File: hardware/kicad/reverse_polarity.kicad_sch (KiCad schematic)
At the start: 4 parts, among them J1 12V_IN, Q1 IRF4905

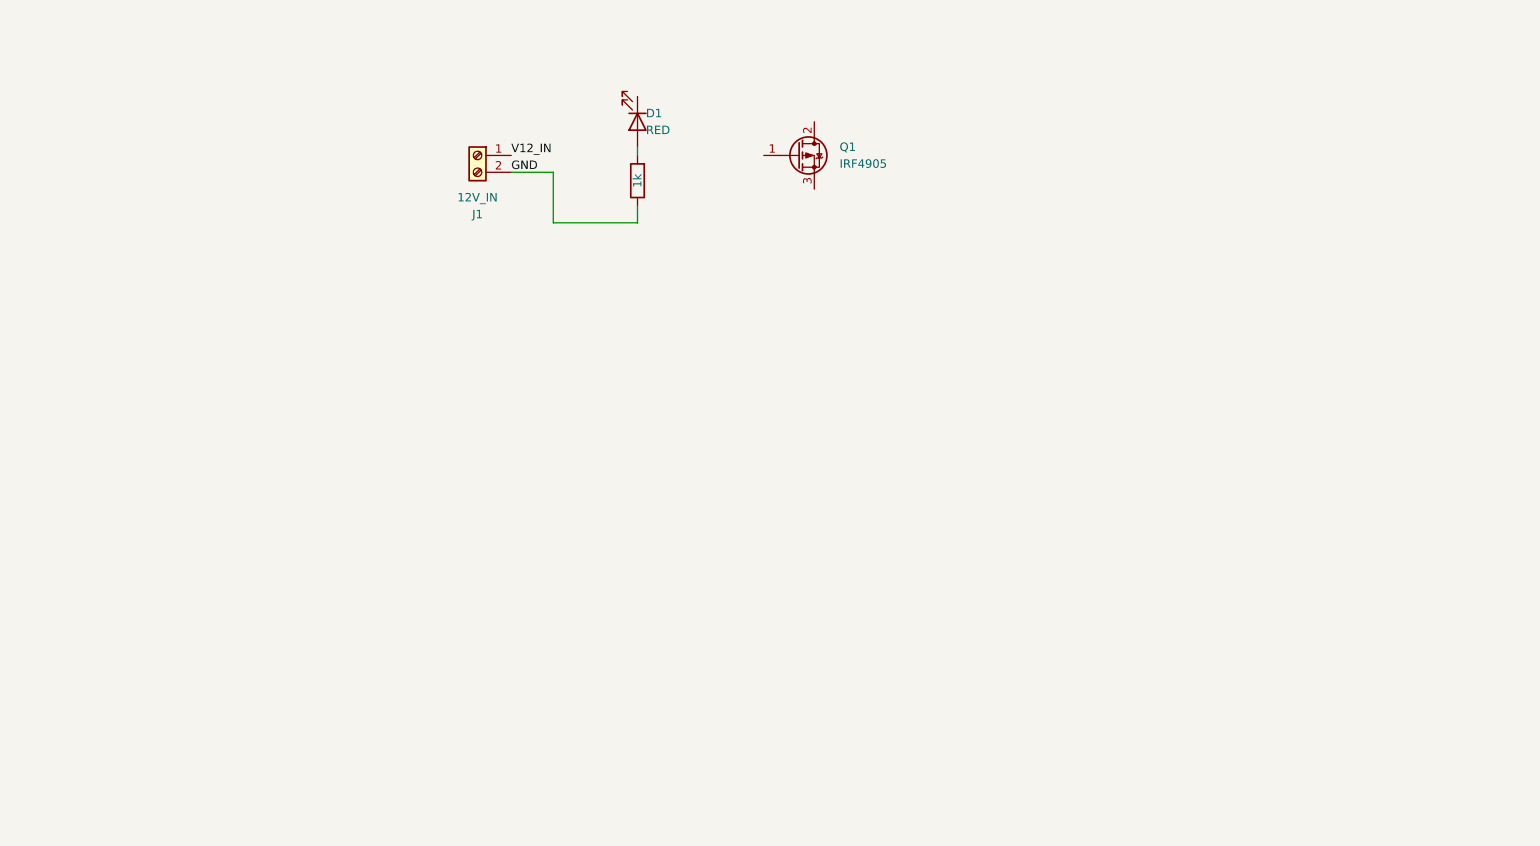
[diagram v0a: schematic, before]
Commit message: feat: implemented schematics of protection
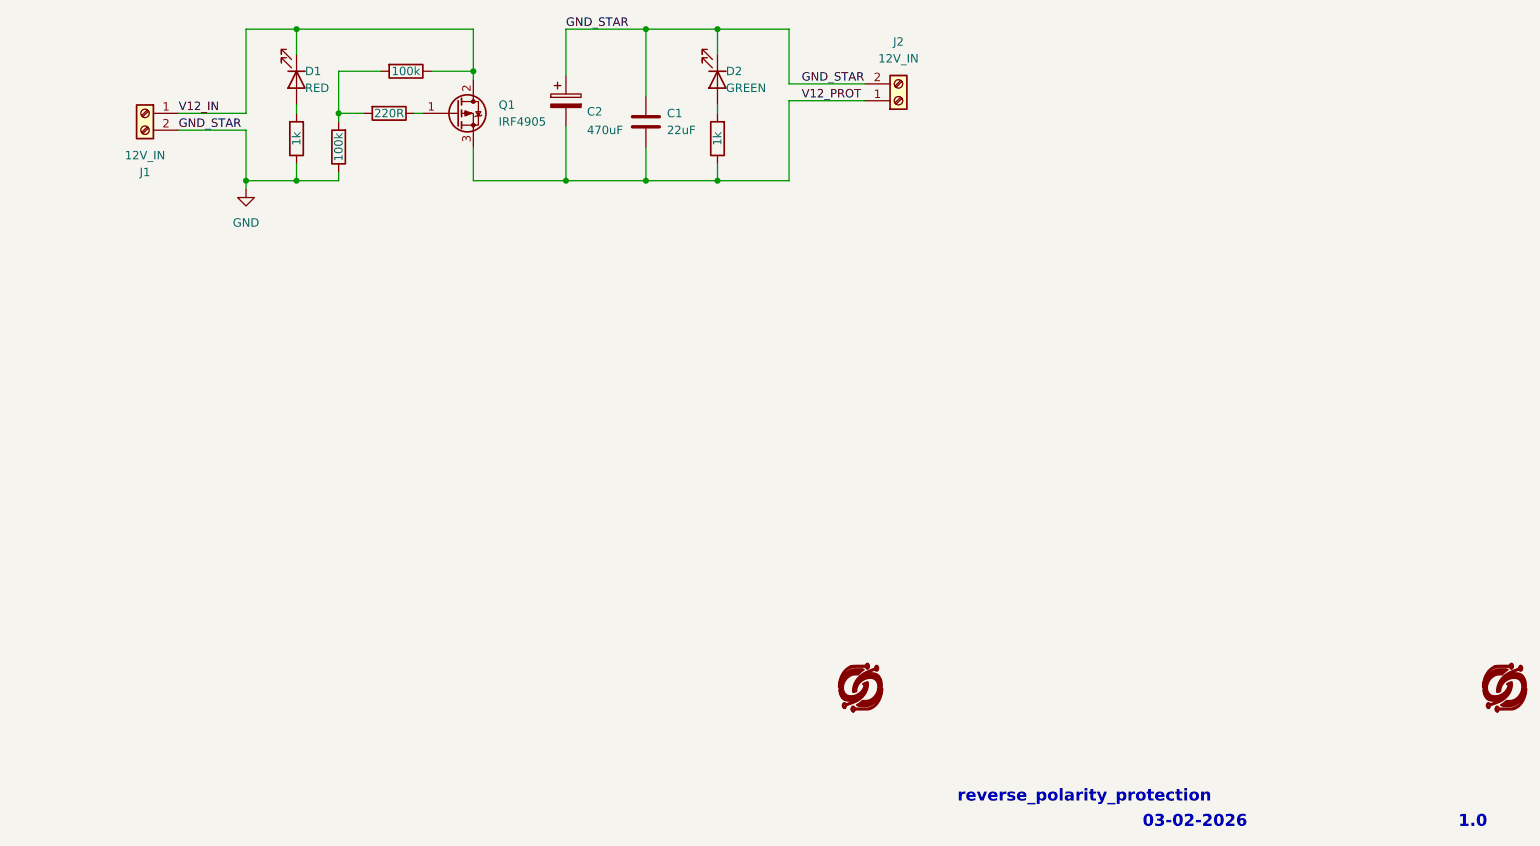
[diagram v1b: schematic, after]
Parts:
- added C1: 22uF, symbol Device:C
- added C2: 470uF, symbol Device:C_Polarized
- added D2: GREEN, symbol Device:LED
- added J2: 12V_IN, symbol Connector:Screw_Terminal_01x02
- added R2: 220R, symbol Device:R
- added R3, R4: 100k, symbol Device:R
- added R5: 1k, symbol Device:R
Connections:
- net GND: now also C1.1, C2.1, D2.1 (K), J2.2 (Pin_2), R4.1
- net V12_IN: now also D1.1 (K), Q1.2 (D), R3.1
- net at Q1.1 (G): now also R2.1
- net V12_PROT: now reaches Q1.3 (S)
- net V12_PROT: now also C1.2, C2.2, J2.1 (Pin_1), R5.1
- new net: R2.2, R3.2, R4.2
- new net: D2.2 (A), R5.2
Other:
- note added: "03-02-2026"
- note added: "1.0"
- note added: "reverse_polarity_protection"
- moved on the sheet: D1, J1, Q1

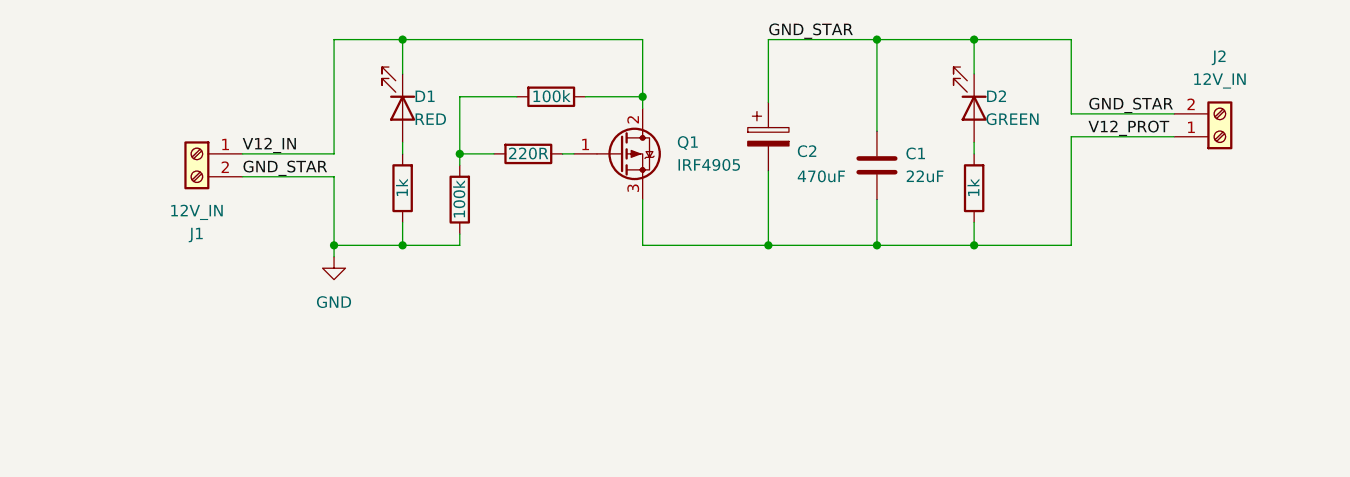
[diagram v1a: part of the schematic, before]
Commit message: perf: refined protection circuit
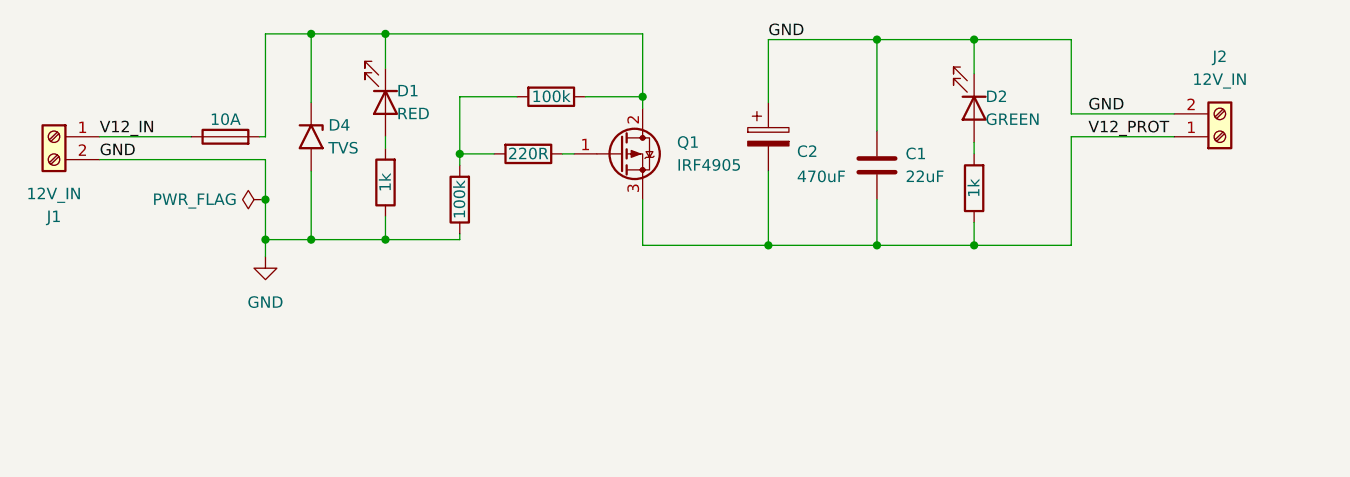
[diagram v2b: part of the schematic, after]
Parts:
- added D4: TVS, Diode_THT:D_DO-201AE_P15.24mm_Horizontal, symbol Diode:1.5KExxA
- added F1: 10A, symbol Device:Fuse
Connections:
- net GND: now also D4.2 (A2)
- net V12_IN: now also F1.1; no longer D1.1 (K), Q1.2 (D), R3.1
- new net: D1.1 (K), D4.1 (A1), F1.2, Q1.2 (D), R3.1
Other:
- moved on the sheet: D1, J1
